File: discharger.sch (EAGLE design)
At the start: 73 parts, among them U1 BW6101, U10 BW6101, U11 BW6101, U12 BW6101, U2 BW6101, U3 BW6101, U4 BW6101, U5 BW6101, U6 BW6101, U7 BW6101, U8 BW6101, U9 BW6101

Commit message: more layout, update pdf
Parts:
- added C1, C10, C11, C12, C2, C3, C4, C5, C6, C7, C8, C9: 0.1uF, resistor:C-EUC0603
- R12, R15, R18, R21, R24, R27, R3, R30, R33, R36, R6, R9: device resistor:R-US_R0805W -> resistor:R-US_R0603
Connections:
- net B-: now also C1.2
- net B1: now also C1.1, C2.2
- net B10: now also C10.1, C11.2
- net B11: now also C11.1, C12.2
- net B12: now also C12.1
- net B2: now also C2.1, C3.2
- net B3: now also C3.1, C4.2
- net B4: now also C4.1, C5.2
- net B5: now also C5.1, C6.2
- net B6: now also C6.1, C7.2
- net B7: now also C7.1, C8.2
- net B8: now also C8.1, C9.2
- net B9: now also C10.2, C9.1
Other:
- moved on the sheet: LED10, LED11, LED12, LED7, LED8, LED9, R19, R20, R21, R22, R23, R24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

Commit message: layout tweaks
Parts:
- LED1, LED10, LED11, LED12, LED2, LED3, LED4, LED5, LED6, LED7, LED8, LED9: device led:LEDCHIP-LED0805 -> led:LEDCHIP-LED0603
- R1, R10, R16, R19, R22, R25, R28, R31, R34, R4, R7: device resistor:R-US_R0805W -> resistor:R-US_R0603

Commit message: tweaks
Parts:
- C1, C10, C11, C12, C2, C3, C4, C5, C6, C7, C8, C9: device resistor:C-EUC0603 -> resistor:C-EUC0805
- LED1, LED10, LED11, LED12, LED2, LED3, LED4, LED5, LED6, LED7, LED8, LED9: device led:LEDCHIP-LED0603 -> led:LEDCHIP-LED0805
- R1, R10, R12, R15, R16, R18, R19, R21, R22, R24, R25, R27, R28, R3, R30, R31, R33, R34, R36, R4, R6, R7, R9: device resistor:R-US_R0603 -> resistor:R-US_R0805
- R13: device resistor:R-US_R0805W -> resistor:R-US_R0805

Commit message: use 2512 resistors to dissipate more power
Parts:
- R11, R14, R17, R2, R20, R23, R26, R29, R32, R35, R5, R8: device resistor:R-US_R1206W -> resistor:R-US_R2512

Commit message: bump version, minor changes
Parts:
- C1, C10, C11, C12, C2, C3, C4, C5, C6, C7, C8, C9: LCSCPART# (none) -> C49678
- LED1, LED10, LED11, LED12, LED2, LED3, LED4, LED5, LED6, LED7, LED8, LED9: device led:LEDCHIP-LED0805 -> led:LEDSML0805; LCSCPART# (none) -> C84256
- R1, R10, R13, R16, R19, R22, R25, R28, R31, R34, R4, R7: LCSCPART# (none) -> C17408
- R11, R14, R17, R2, R20, R23, R26, R29, R32, R35, R5, R8: LCSCPART# (none) -> C25384
- R12, R15, R18, R21, R24, R27, R3, R30, R33, R36, R6, R9: LCSCPART# (none) -> C17513

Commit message: updates
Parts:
- added LED13, LED14, LED15, LED16, LED17, LED18, LED19, LED20, LED21, LED22, LED23, LED24: ALARM, led:LEDSML0805
- added R37, R38, R39, R40, R41, R42, R43, R44, R45, R46, R47, R48: 1K, resistor:R-US_R0805
- C1, C10, C11, C12, C2, C3, C4, C5, C6, C7, C8, C9: device resistor:C-EUC0805 -> resistor:C-EUC0603
- LED1, LED10, LED11, LED12, LED2, LED3, LED4, LED5, LED6, LED7, LED8, LED9: value ALARM -> BLEED
- R1, R10, R4, R7: value 100R -> 47R; device resistor:R-US_R0805 -> resistor:R-US_R2512; LCSCPART# C17408 -> C25384
- R12, R3, R6, R9: value 1K -> 47R; device resistor:R-US_R0805 -> resistor:R-US_R2512; LCSCPART# C17513 -> C25384
- R14, R17, R20, R23, R26, R29, R32, R35: value 47R -> 100R; device resistor:R-US_R2512 -> resistor:R-US_R0805; LCSCPART# C25384 -> C17408
- R15, R18, R21, R24, R27, R30, R33, R36: value 1K -> 100R; LCSCPART# C17513 -> C17408
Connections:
- new net N$1: R1.1, R13.1, U1.IOUT
- new net N$2: LED1.A, R13.2
- new net N$3: R25.1, U1.LED
- new net N$31: LED10.A, R22.2
- new net N$32: LED11.A, R23.2
- new net N$33: LED12.A, R24.2
- new net N$34: LED6.A, R18.2
- new net N$35: LED5.A, R17.2
- new net N$4: LED2.A, R14.2
- new net N$51: LED4.A, R16.2
- new net N$52: LED3.A, R15.2
- new net N$60: LED19.A, R31.2
- net B-: now also LED13.C, R1.2; no longer R2.2
- net B1: now also LED14.C, R2.2, R37.1; no longer R3.1, R5.2
- net B10: now also LED23.C, R11.2, R46.1; no longer R30.1, R32.2
- net B11: now also LED24.C, R12.2, R47.1; no longer R33.1, R35.2
- net B12: now also R48.1; no longer R36.1
- net B2: now also LED15.C, R3.2, R38.1; no longer R6.1, R8.2
- net B3: now also LED16.C, R39.1, R4.2; no longer R11.2, R9.1
- net B4: now also LED17.C, R40.1, R5.2; no longer R12.1, R14.2
- net B5: now also LED18.C, R41.1, R6.2; no longer R15.1, R17.2
- net B6: now also LED19.C, R42.1, R7.2; no longer R18.1, R20.2
- net B7: now also LED20.C, R43.1, R8.2; no longer R21.1, R23.2
- net B8: now also LED21.C, R44.1, R9.2; no longer R24.1, R26.2
- net B9: now also LED22.C, R10.2, R45.1; no longer R27.1, R29.2
- net N$10: now also LED15.A, R27.2; no longer LED3.A, R7.2
- net N$11: now also LED8.A, R20.2; no longer R2.1, U1.IOUT
- net N$13: now also R37.2; no longer R3.2
- net N$14: now also LED9.A, R21.2; no longer R1.1, U1.LED
- net N$15: now also LED13.A, R25.2; no longer LED1.A, R1.2
- net N$16: now also R20.1, R8.1; no longer R23.1
- net N$18: now also R44.2; no longer R24.2
- net N$19: now also R32.1; no longer R22.1
- net N$20: now also LED20.A, R32.2; no longer LED8.A, R22.2
- net N$21: now also R14.1, R2.1; no longer R5.1
- net N$23: now also R38.2; no longer R6.2
- net N$24: now also R26.1; no longer R4.1
- net N$25: now also LED14.A, R26.2; no longer LED2.A, R4.2
- net N$26: now also R16.1, R4.1; no longer R11.1
- net N$28: now also R40.2; no longer R12.2
- net N$29: now also R28.1; no longer R10.1
- net N$30: now also LED16.A, R28.2; no longer LED4.A, R10.2
- net N$36: now also R17.1, R5.1; no longer R14.1
- net N$38: now also R41.2; no longer R15.2
- net N$39: now also R29.1; no longer R13.1
- net N$40: now also LED17.A, R29.2; no longer LED5.A, R13.2
- net N$41: now also R21.1, R9.1; no longer R26.1
- net N$43: now also R45.2; no longer R27.2
- net N$44: now also R33.1; no longer R25.1
- net N$45: now also LED21.A, R33.2; no longer LED9.A, R25.2
- net N$46: now also R18.1, R6.1; no longer R17.1
- net N$48: now also R42.2; no longer R18.2
- net N$49: now also R30.1; no longer R16.1
- net N$50: now also LED18.A, R30.2; no longer LED6.A, R16.2
- net N$56: now also R19.1, R7.1; no longer R20.1
- net N$58: now also R43.2; no longer R21.2
- net N$59: now also R31.1; no longer R19.1
- net N$6: now also R15.1, R3.1; no longer R8.1
- net N$61: now also R10.1, R22.1; no longer R29.1
- net N$63: now also R46.2; no longer R30.2
- net N$64: now also R34.1; no longer R28.1
- net N$65: now also LED22.A, R34.2; no longer LED10.A, R28.2
- net N$71: now also R11.1, R23.1; no longer R32.1
- net N$73: now also R47.2; no longer R33.2
- net N$74: now also R35.1; no longer R31.1
- net N$75: now also LED23.A, R35.2; no longer LED11.A, R31.2
- net N$8: now also R39.2; no longer R9.2
- net N$81: now also R12.1, R24.1; no longer R35.1
- net N$83: now also R48.2; no longer R36.2
- net N$84: now also R36.1; no longer R34.1
- net N$85: now also LED24.A, R36.2; no longer LED12.A, R34.2
- net N$9: now also R27.1; no longer R7.1
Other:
- moved on the sheet: C10, C11, C12, C7, C8, C9, JP1, LED1, LED10, LED11, LED12, LED2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

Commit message: move 1k resistor onto SEL side of jumper
more fiddling
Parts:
- R13, R14, R15, R16, R17, R18, R19, R20, R21, R22, R23, R24, R25, R26, R27, R28, R29, R30, R31, R32, R33, R34, R35, R36: device resistor:R-US_R0805 -> resistor:R-US_R0603
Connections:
- removed net N$72: SJ11.2, U11.SEL
- removed net N$73: R47.2, SJ11.3
- removed net N$82: SJ12.2, U12.SEL
- removed net N$83: R48.2, SJ12.3
- new net N$53: R44.2, U8.SEL
- new net N$54: R43.2, U7.SEL
- new net N$55: R42.2, U6.SEL
- new net N$66: R37.2, U1.SEL
- net B1: now also SJ1.3; no longer R37.1
- net B10: now also SJ10.3; no longer R46.1
- net B11: now also SJ11.3; no longer R47.1
- net B12: now also SJ12.3; no longer R48.1
- net B2: now also SJ2.3; no longer R38.1
- net B3: now also SJ3.3; no longer R39.1
- net B4: now also SJ4.3; no longer R40.1
- net B5: now also SJ5.3; no longer R41.1
- net B6: now also SJ6.3; no longer R42.1
- net B7: now also SJ7.3; no longer R43.1
- net B8: now also SJ8.3; no longer R44.1
- net B9: now also SJ9.3; no longer R45.1
- net N$12: now also R39.1, SJ3.2; no longer SJ1.2, U1.SEL
- net N$13: now also R40.1, SJ4.2; no longer R37.2, SJ1.3
- net N$17: now also R41.1, SJ5.2; no longer SJ8.2, U8.SEL
- net N$18: now also R42.1, SJ6.2; no longer R44.2, SJ8.3
- net N$22: now also R43.1, SJ7.2; no longer SJ2.2, U2.SEL
- net N$23: now also R44.1, SJ8.2; no longer R38.2, SJ2.3
- net N$27: now also R45.1, SJ9.2; no longer SJ4.2, U4.SEL
- net N$28: now also R46.1, SJ10.2; no longer R40.2, SJ4.3
- net N$37: now also R47.1, SJ11.2; no longer SJ5.2, U5.SEL
- net N$38: now also R48.1, SJ12.2; no longer R41.2, SJ5.3
- net N$42: now also R48.2, U12.SEL; no longer SJ9.2, U9.SEL
- net N$43: now also R47.2, U11.SEL; no longer R45.2, SJ9.3
- net N$47: now also R46.2, U10.SEL; no longer SJ6.2, U6.SEL
- net N$48: now also R45.2, U9.SEL; no longer R42.2, SJ6.3
- net N$57: now also R41.2, U5.SEL; no longer SJ7.2, U7.SEL
- net N$58: now also R40.2, U4.SEL; no longer R43.2, SJ7.3
- net N$62: now also R39.2, U3.SEL; no longer SJ10.2, U10.SEL
- net N$63: now also R38.2, U2.SEL; no longer R46.2, SJ10.3
- net N$7: now also R37.1, SJ1.2; no longer SJ3.2, U3.SEL
- net N$8: now also R38.1, SJ2.2; no longer R39.2, SJ3.3
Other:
- moved on the sheet: C1, C10, C11, C12, C2, C3, C4, C5, C6, C7, C8, C9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

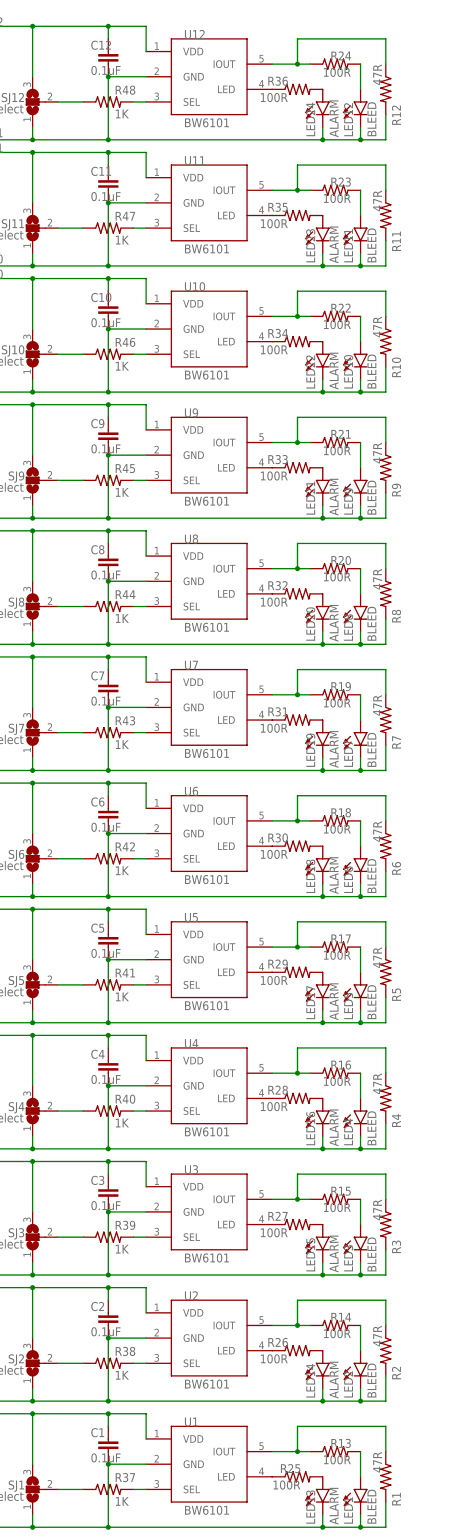
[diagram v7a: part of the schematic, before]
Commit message: custom parts for LEDs, misc fixes
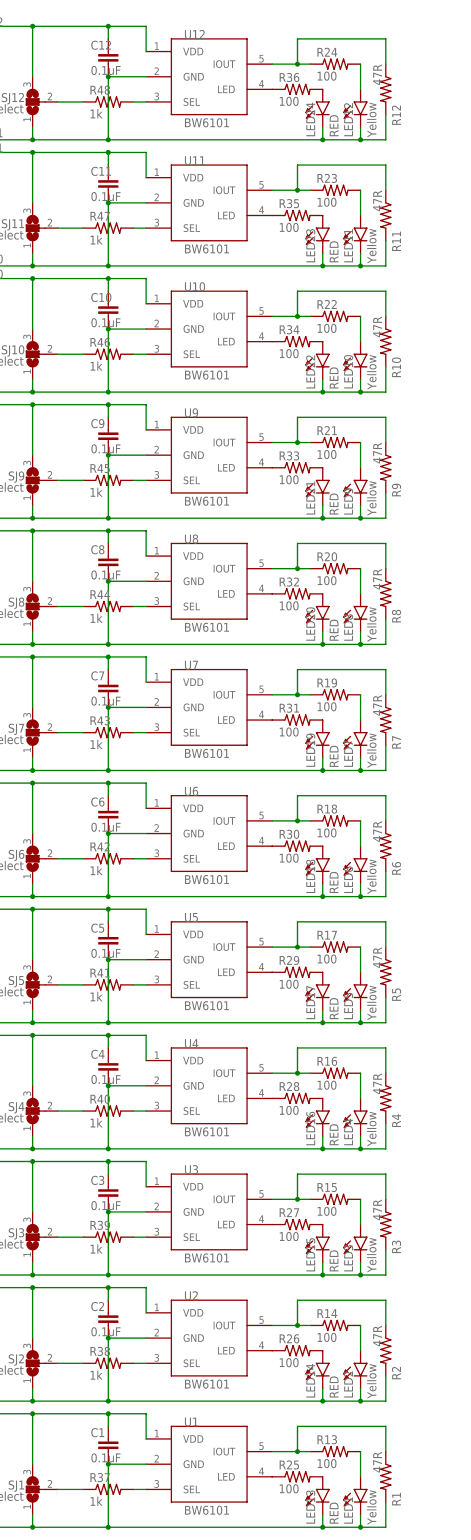
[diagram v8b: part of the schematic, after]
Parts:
- LED1, LED10, LED11, LED12, LED2, LED3, LED4, LED5, LED6, LED7, LED8, LED9: value BLEED -> Yellow; device led:LEDSML0805 -> ltobms:LED-YELLOW0603
- LED13, LED14, LED15, LED16, LED17, LED18, LED19, LED20, LED21, LED22, LED23, LED24: value ALARM -> RED; device led:LEDSML0805 -> ltobms:LED-RED0603
- R13, R14, R15, R16, R17, R18, R19, R20, R21, R22, R23, R24, R25, R26, R27, R28, R29, R30, R31, R32, R33, R34, R35, R36: value 100R -> 100
- R37, R38, R39, R40, R41, R42, R43, R44, R45, R46, R47, R48: value 1K -> 1k; device resistor:R-US_R0805 -> resistor:R-US_R0603
